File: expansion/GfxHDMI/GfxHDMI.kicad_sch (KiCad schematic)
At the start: 10 parts, among them J101 D68K_64PIN_BOARD, U101 SN74LS125ADR, U102 LD1117S12TR_SOT223

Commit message: Working on some new GFX ideas
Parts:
- U101: value SN74LS125ADR -> 74LS125
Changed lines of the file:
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@@
       (effects (font (size 1.27 1.27)))
     )
-    (property "Value" "SN74LS125ADR" (at 76.2 169.5196 0)
+    (property "Value" "74LS125" (at 76.2 169.5196 0)
       (effects (font (size 1.27 1.27)))
     )
@@
       (effects (font (size 1.27 1.27)))
     )
-    (property "Value" "SN74LS125ADR" (at 139.7 146.6596 0)
+    (property "Value" "74LS125" (at 139.7 146.6596 0)
       (effects (font (size 1.27 1.27)))
     )
@@
       (effects (font (size 1.27 1.27)))
     )
-    (property "Value" "SN74LS125ADR" (at 139.7 165.7096 0)
+    (property "Value" "74LS125" (at 139.7 165.7096 0)
       (effects (font (size 1.27 1.27)))
     )
@@
       (effects (font (size 1.27 1.27)))
     )
-    (property "Value" "SN74LS125ADR" (at 55.88 169.5196 0)
+    (property "Value" "74LS125" (at 55.88 169.5196 0)
       (effects (font (size 1.27 1.27)))
     )
@@
       (effects (font (size 1.27 1.27)) (justify left))
     )
-    (property "Value" "SN74LS125ADR" (at 239.522 158.623 0)
+    (property "Value" "74LS125" (at 239.522 158.623 0)
       (effects (font (size 1.27 1.27)) (justify left))
     )

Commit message: More work on the HDMI board
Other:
- sheet FPGA ports: added HDMI_TX0_N, HDMI_TX0_P, HDMI_TX1_N, HDMI_TX1_P, HDMI_TX2_N, HDMI_TX2_P, HDMI_TXC_N, HDMI_TXC_P; removed B[0..7], G[0..7], HSYNC, PIXELCLOCK, R[0..7], VSYNC, ~{BLANK}
- sheet VGA ports: added HDMI_TX0_N, HDMI_TX0_P, HDMI_TX1_N, HDMI_TX1_P, HDMI_TX2_N, HDMI_TX2_P, HDMI_TXC_N, HDMI_TXC_P; removed B[0..7], G[0..7], HSYNC, PIXELCLOCK, R[0..7], VSYNC, ~{BLANK}

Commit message: minor changes
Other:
- sheet VGA renamed HDMI
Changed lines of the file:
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@@
     (stroke (width 0) (type solid))
     (fill (color 0 0 0 0.0000))
-    (property "Sheetname" "VGA" (at 247.65 93.2684 0)
+    (property "Sheetname" "HDMI" (at 247.65 93.2684 0)
       (effects (font (size 1.27 1.27)) (justify left bottom))
     )

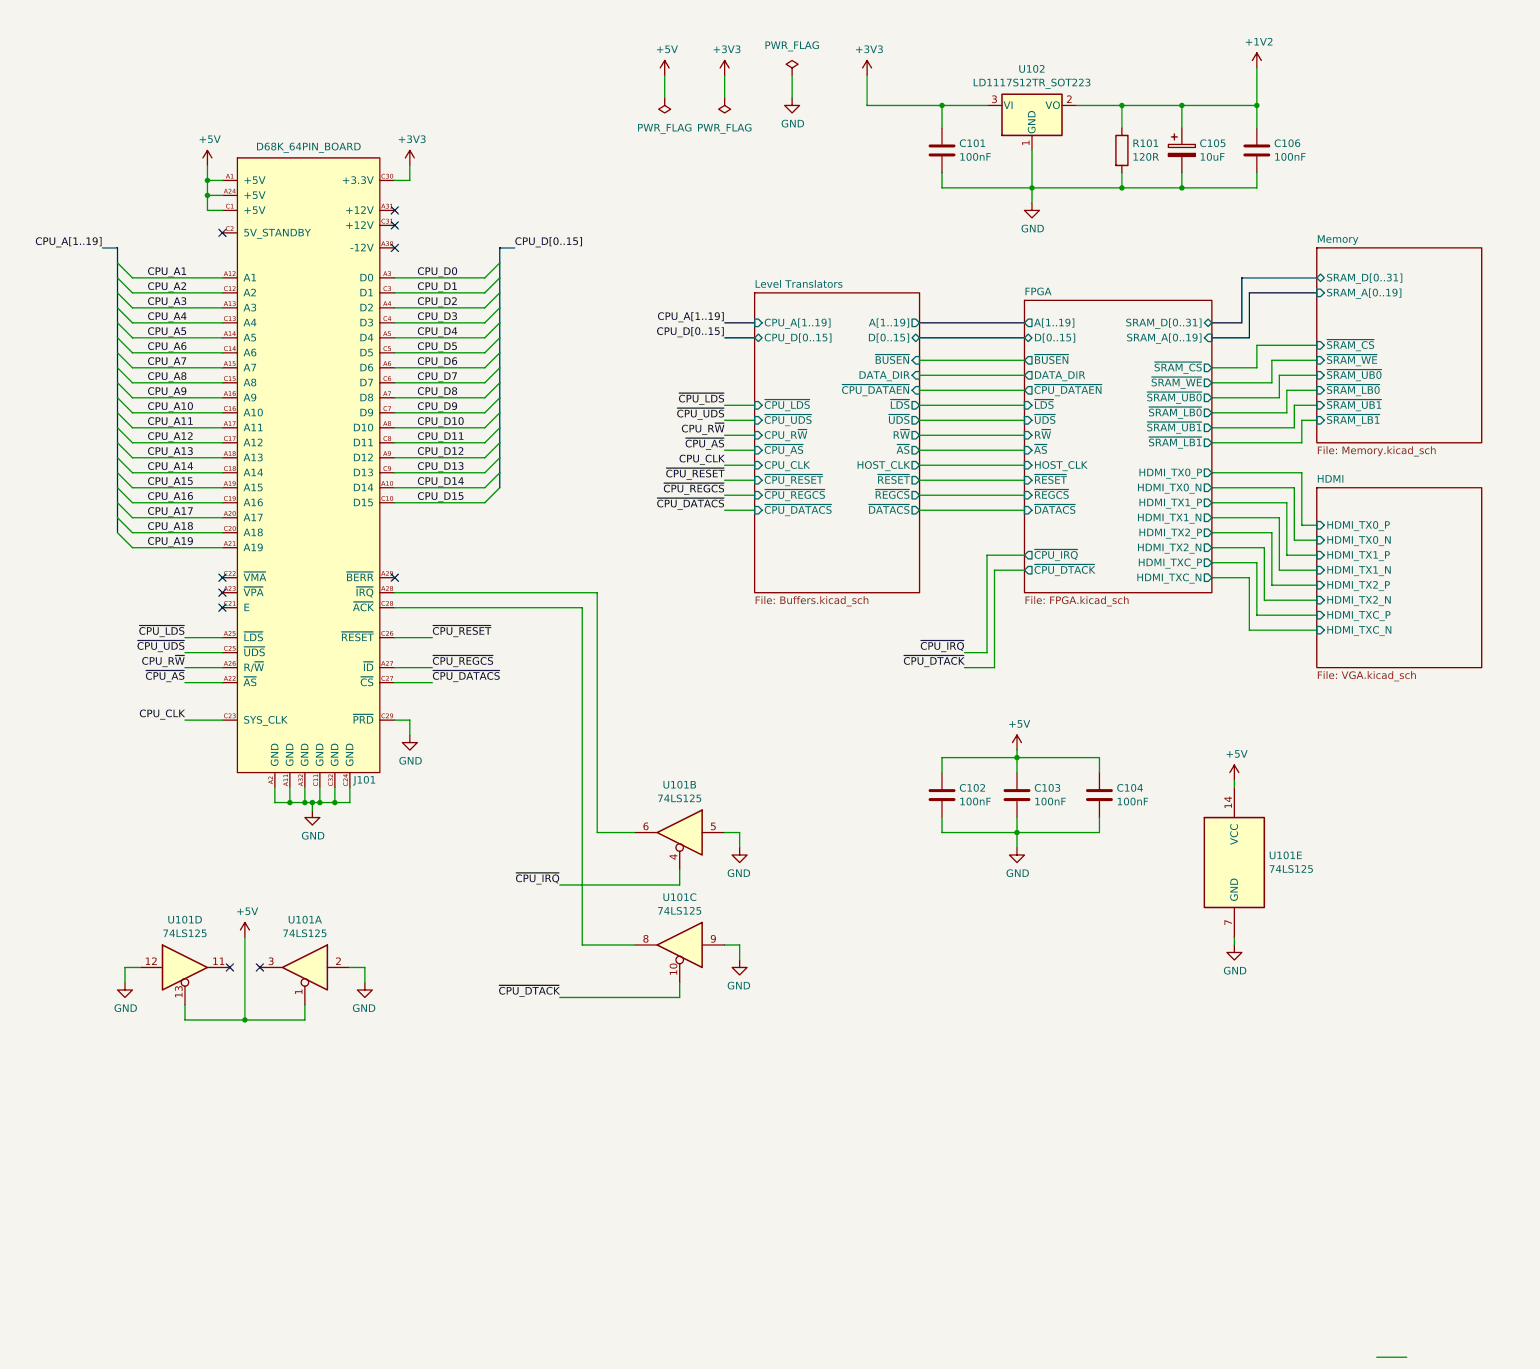
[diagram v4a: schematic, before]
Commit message: Added HDMI card based on VGA design
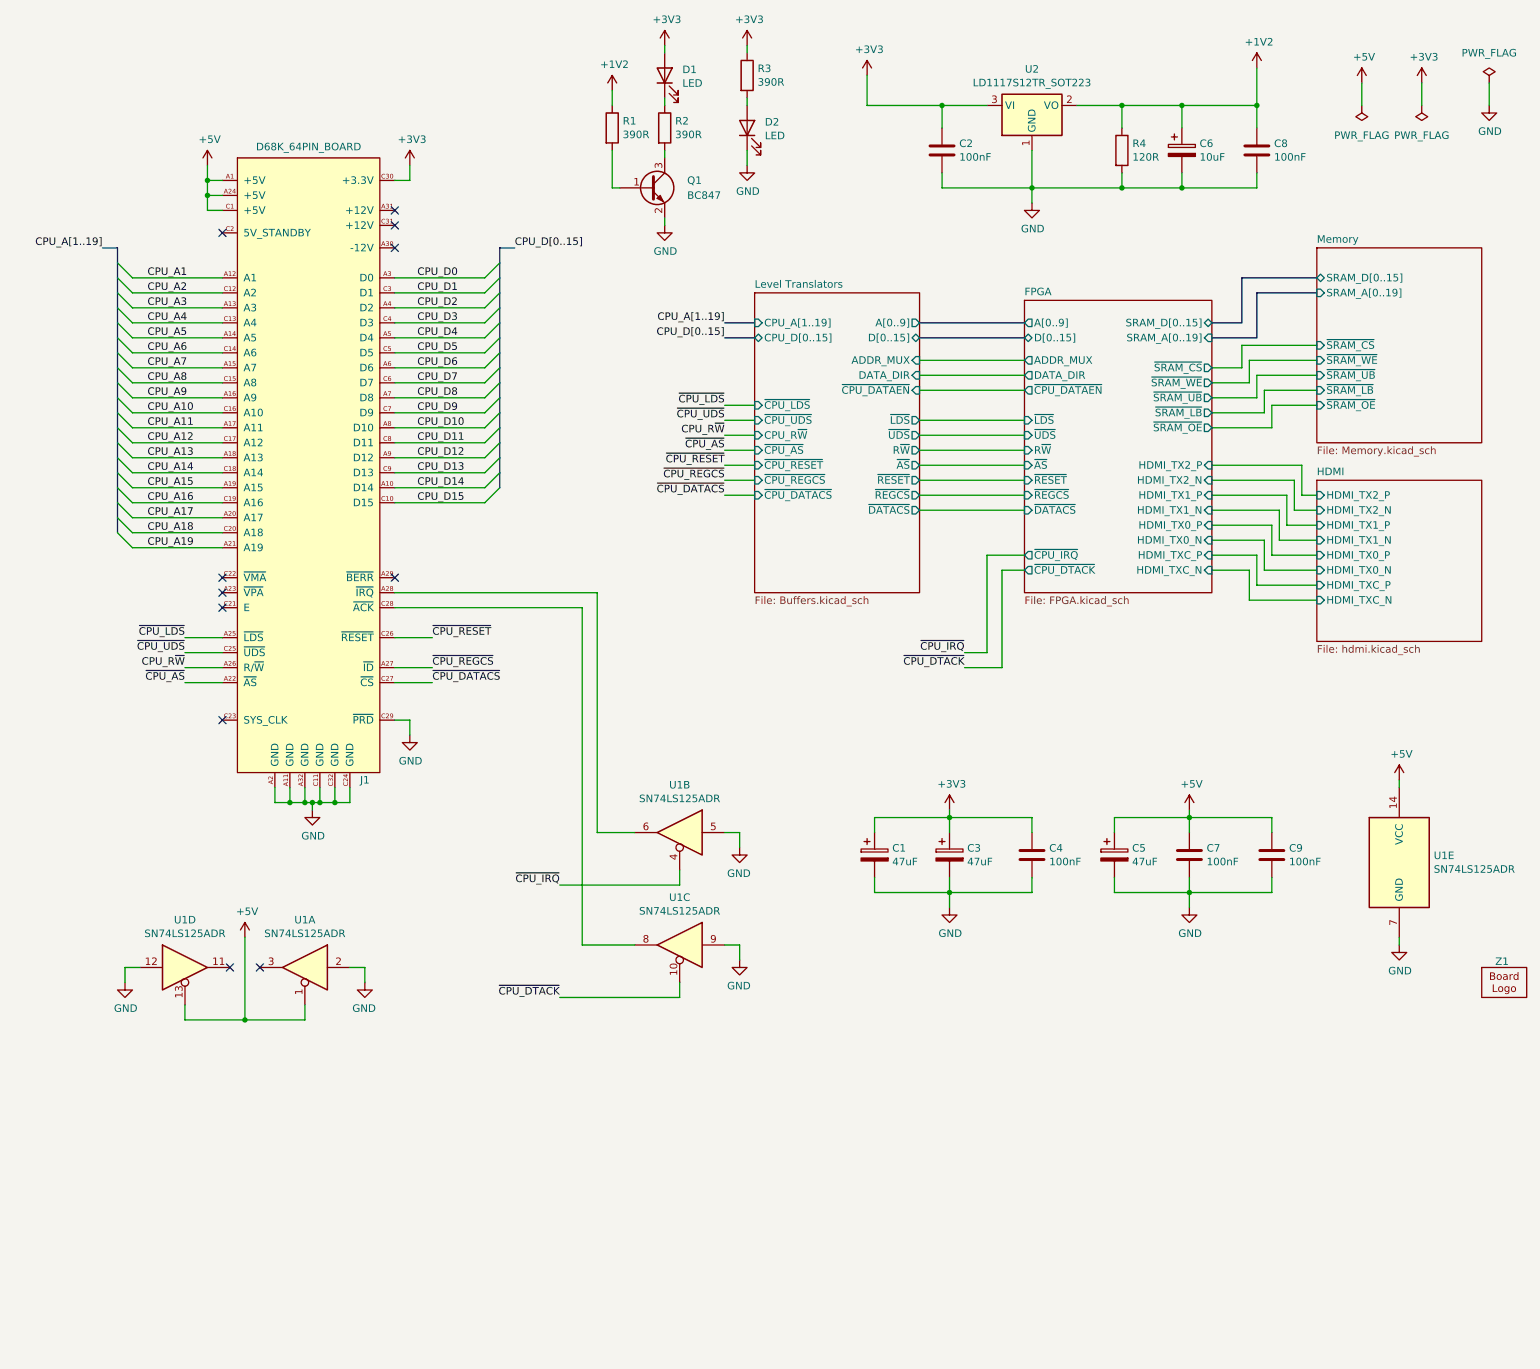
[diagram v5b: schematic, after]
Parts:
- removed C102: 100nF, Capacitor_SMD:C_0805_2012Metric, symbol Device:C
- added C1, C3, C5: 47uF, Capacitor_SMD:CP_Elec_4x5.3, symbol Device:C_Polarized
- added C4: 100nF, Capacitor_SMD:C_0805_2012Metric, symbol Device:C
- added D1, D2: LED, LED_SMD:LED_1206_3216Metric, symbol Device:LED
- added Q1: BC847, Package_TO_SOT_SMD:SOT-23, symbol Transistor_BJT:BC847
- added R1, R2, R3: 390R, Resistor_SMD:R_0805_2012Metric, symbol Device:R
- added Z1: ~, Ddraig:Ddraig68k-26mm, symbol Ddraig:DdraigLogo
- U1: renamed from U101; value 74LS125 -> SN74LS125ADR
- renumbered C101 to C2, C105 to C6, C103 to C7, C106 to C8, C104 to C9, J101 to J1, R101 to R4, U102 to U2
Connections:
- net +1V2: now also R1.1
- net +3V3: now also C1.1, C3.1, C4.1, D1.2 (A), R3.1
- net +5V: now also C5.1
- net GND: now also C1.2, C3.2, C4.2, C5.2, D2.1 (K), Q1.2 (E)
- net CPU_CLK: no longer names the net of J1.C23 (SYS_CLK)
- new net: Q1.1 (B), R1.2
- new net: D1.1 (K), R2.1
- new net: Q1.3 (C), R2.2
- new net: D2.2 (A), R3.2
- no-connect marks 10 -> 11
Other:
- sheet FPGA ports: added ADDR_MUX, A[0..9], SRAM_D[0..15], ~{SRAM_LB}, ~{SRAM_OE}, ~{SRAM_UB}; removed A[1..19], HOST_CLK, SRAM_D[0..31], ~{BUSEN}, ~{SRAM_LB0}, ~{SRAM_LB1}, ~{SRAM_UB0}, ~{SRAM_UB1}
- sheet HDMI: file VGA.kicad_sch -> hdmi.kicad_sch
- sheet Level Translators ports: added ADDR_MUX, A[0..9]; removed A[1..19], CPU_CLK, HOST_CLK, ~{BUSEN}
- sheet Memory ports: added SRAM_D[0..15], ~{SRAM_LB}, ~{SRAM_OE}, ~{SRAM_UB}; removed SRAM_D[0..31], ~{SRAM_LB0}, ~{SRAM_LB1}, ~{SRAM_UB0}, ~{SRAM_UB1}
- moved on the sheet: C7, C9, U1E
